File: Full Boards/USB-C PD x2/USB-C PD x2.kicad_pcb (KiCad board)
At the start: 4 copper layers, 96 x 136 mm, 161 parts, among them J1 Conn_02x05_Odd_Even, J2 Conn_01x05_Pin

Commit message: Changed the over voltage on the PMIC to under-voltage below 8.15V and over-voltage at 17.0V via a new voltage divider. This should save the TVS if the board is connected to a 24v supply.
Signed-off-by: digimer <digital.mermaid@gmail.com>
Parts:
- added R26: 47KR, Resistor_SMD:R_1206_3216Metric, F.Cu at (108.1, 153.2)
- R2: value 100KR -> 51.1KR
- TR1, TR10, TR11, TR12, TR2, TR3, TR4, TR5, TR6, TR7, TR8, TR9: value SOIC8_DMTH45M5LPSWQ-13_DIO -> Diodes Inc DMTH45M5LPSWQ-13
- moved R1 0.70 mm to (108.1, 148.6)
- moved R2 0.70 mm to (108.1, 150.9)
- moved C1 0.20 mm to (105.2, 155.5)
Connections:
- PMIC1 pad 3: -BATT -> Net-(PMIC1-OV)
- R2 pad 1: -BATT -> Net-(PMIC1-OV)
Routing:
- net Net-(PMIC1-OV): track 0.00 -> 16.2 mm
- net -BATT: track 100.8 -> 99.3 mm, vias 202 -> 200
- net Net-(HS1-D): track 46.8 -> 47.8 mm

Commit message: Updated PCB to apply the resistor KR -> kR corrections
Signed-off-by: digimer <digital.mermaid@gmail.com>
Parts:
- PR1, PR2, Rc2: value 2.2KR -> 2.2kR
- R17, R18, R19, R24: value 10KR -> 10kR
- R2: value 51.1KR -> 51.1kR
- R25: value xKR -> xkR
- R26: value 47KR -> 47kR
- R3: value 22.1KR -> 22.1kR
- Rc1: value 20KR -> 20kR
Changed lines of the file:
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@@
 			)
 		)
-		(property "Value" "22.1KR"
+		(property "Value" "22.1kR"
 			(at 0 1.83 0)
 			(layer "F.Fab")
@@
 			)
 		)
-		(property "Datasheet" ""
+		(property "Datasheet" "https://www.seielect.com/catalog/SEI-RNCP.pdf"
 			(at 0 0 0)
 			(layer "F.Fab")
@@
 			)
 		)
-		(property "Description" "RNCP1206FTD100K 100KR 0.5W"
+		(property "Description" "22.1 kOhms ±1% 0.5W, 1/2W Chip Resistor 1206 (3216 Metric) Anti-Sulfur Thin Film"
 			(at 0 0 0)
 			(layer "F.Fab")
@@
 			)
 		)
+		(property "Part" "Stackpole RNCP1206FTD22K1"
+			(at 0 0 180)
+			(unlocked yes)
+			(layer "F.Fab")
+			(hide yes)
+			(effects
+				(font
+					(size 1 1)
+					(thickness 0.15)
+				)
+			)
+		)
 		(property ki_fp_filters "R_*")
 		(sheetname "/")
@@
 			)
 		)
-		(property "Value" "10KR"
+		(property "Value" "10kR"
 			(at 0 1.83 90)
 			(layer "F.Fab")
@@
 			)
 		)
-		(property "Value" "2.2KR"
+		(property "Value" "2.2kR"
 			(at 0 1.83 0)
 			(layer "F.Fab")
@@
 			)
 		)
-		(property "Value" "xKR"
+		(property "Value" "xkR"
 			(at 0 4.1 0)
 			(unlocked yes)
@@
 			)
 		)
-		(property "Value" "2.2KR"
+		(property "Value" "2.2kR"
 			(at 0 1.83 90)
 			(layer "F.Fab")
@@
 			)
 		)
-		(property "Value" "20KR"
+		(property "Value" "20kR"
 			(at 0 1.83 90)
 			(layer "F.Fab")
@@
 			)
 		)
-		(property "Value" "2.2KR"
+		(property "Value" "2.2kR"
 			(at 0 1.83 0)
 			(layer "F.Fab")
@@
 			)
 		)
-		(property "Value" "10KR"
+		(property "Value" "10kR"
 			(at 0 4.1 0)
 			(unlocked yes)
@@
 			)
 		)
-		(property "Value" "47KR"
+		(property "Value" "47kR"
 			(at 0 1.83 0)
 			(layer "F.Fab")
@@
 			)
 		)
-		(property "Value" "51.1KR"
+		(property "Value" "51.1kR"
 			(at 0 1.83 0)
 			(layer "F.Fab")
@@
 			)
 		)
-		(property "Value" "10KR"
+		(property "Value" "10kR"
 			(at 0 1.83 90)
 			(layer "F.Fab")
@@
 			)
 		)
-		(property "Value" "10KR"
+		(property "Value" "10kR"
 			(at 0 1.83 90)
 			(layer "F.Fab")
@@
 	)
 	(segment
+		(start 104 151.79)
+		(end 104 152.8395)
+		(width 0.2)
+		(layer "F.Cu")
+		(net "Net-(PMIC1-OV)")
+	)
+	(segment
+		(start 109.5625 155.2375)
+		(end 109.5625 153.2)
+		(width 0.2)
+		(layer "F.Cu")
+		(net "Net-(PMIC1-OV)")
+	)
+	(segment
+		(start 103.5 156.6)
+		(end 108.2 156.6)
+		(width 0.2)
+		(layer "F.Cu")
+		(net "Net-(PMIC1-OV)")
+	)
+	(segment
+		(start 103.2 156.3)
+		(end 103.5 156.6)
+		(width 0.2)
+		(layer "F.Cu")
+		(net "Net-(PMIC1-OV)")
+	)
+	(segment
+		(start 104 152.8395)
+		(end 103.2 153.6395)
+		(width 0.2)
+		(layer "F.Cu")
+		(net "Net-(PMIC1-OV)")
+	)
+	(segment
+		(start 103.2 153.6395)
+		(end 103.2 156.3)
+		(width 0.2)
+		(layer "F.Cu")
+		(net "Net-(PMIC1-OV)")
+	)
+	(segment
+		(start 109.5625 153.2)
+		(end 109.5625 150.9)
+		(width 0.2)
+		(layer "F.Cu")
+		(net "Net-(PMIC1-OV)")
+	)
+	(segment
+		(start 108.2 156.6)
+		(end 109.5625 155.2375)
+		(width 0.2)
+		(layer "F.Cu")
+		(net "Net-(PMIC1-OV)")
+	)
+	(segment
 		(start 103.5 151.79)
 		(end 103.5 150.85)
@@
 		(net "Net-(TR7-G)")
 	)
-	(segment
-		(start 104 151.79)
-		(end 104 152.8395)
-		(width 0.2)
-		(layer "F.Cu")
-		(net "Net-(PMIC1-OV)")
-	)
-	(segment
-		(start 109.5625 155.2375)
-		(end 109.5625 153.2)
-		(width 0.2)
-		(layer "F.Cu")
-		(net "Net-(PMIC1-OV)")
-	)
-	(segment
-		(start 103.5 156.6)
-		(end 108.2 156.6)
-		(width 0.2)
-		(layer "F.Cu")
-		(net "Net-(PMIC1-OV)")
-	)
-	(segment
-		(start 103.2 156.3)
-		(end 103.5 156.6)
-		(width 0.2)
-		(layer "F.Cu")
-		(net "Net-(PMIC1-OV)")
-	)
-	(segment
-		(start 104 152.8395)
-		(end 103.2 153.6395)
-		(width 0.2)
-		(layer "F.Cu")
-		(net "Net-(PMIC1-OV)")
-	)
-	(segment
-		(start 103.2 153.6395)
-		(end 103.2 156.3)
-		(width 0.2)
-		(layer "F.Cu")
-		(net "Net-(PMIC1-OV)")
-	)
-	(segment
-		(start 109.5625 153.2)
-		(end 109.5625 150.9)
-		(width 0.2)
-		(layer "F.Cu")
-		(net "Net-(PMIC1-OV)")
-	)
-	(segment
-		(start 108.2 156.6)
-		(end 109.5625 155.2375)
-		(width 0.2)
-		(layer "F.Cu")
-		(net "Net-(PMIC1-OV)")
-	)
 	(zone

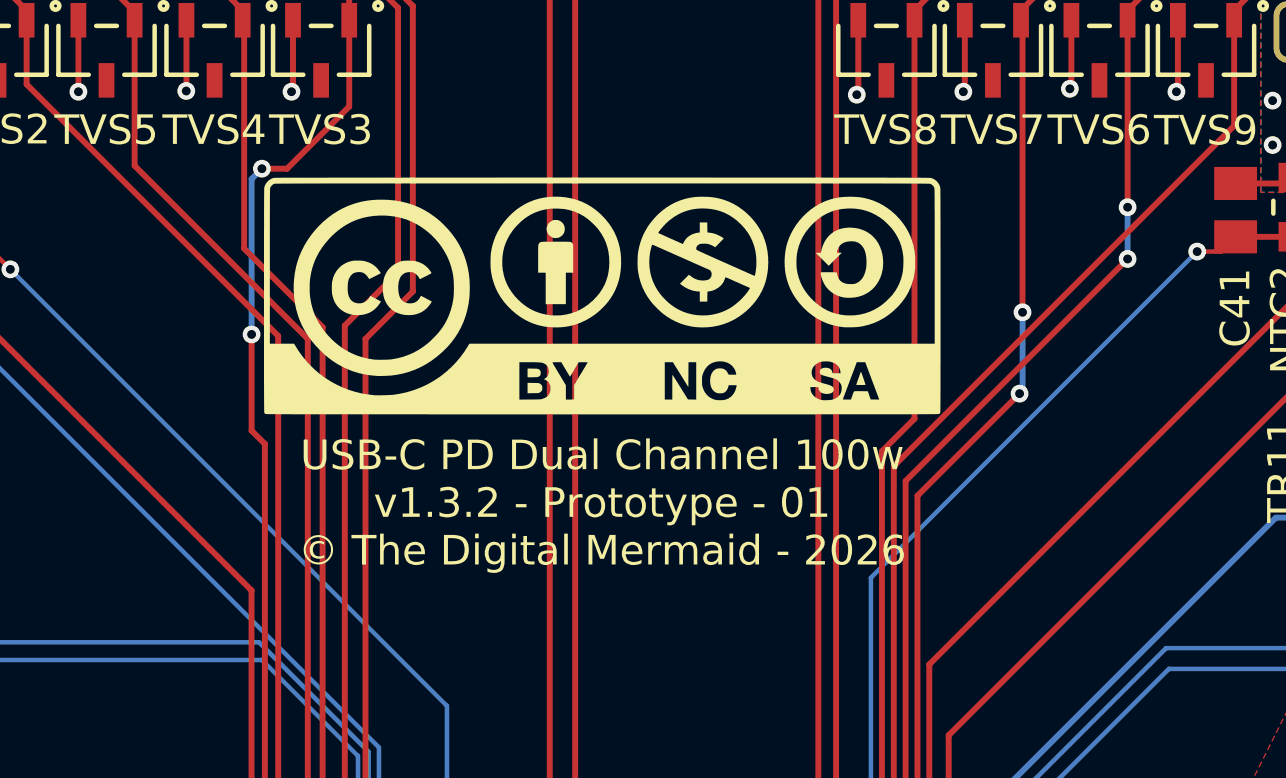
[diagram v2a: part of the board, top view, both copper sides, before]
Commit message: Changed the license to CERN-OHL-W v2.
Signed-off-by: digimer <digital.mermaid@gmail.com>
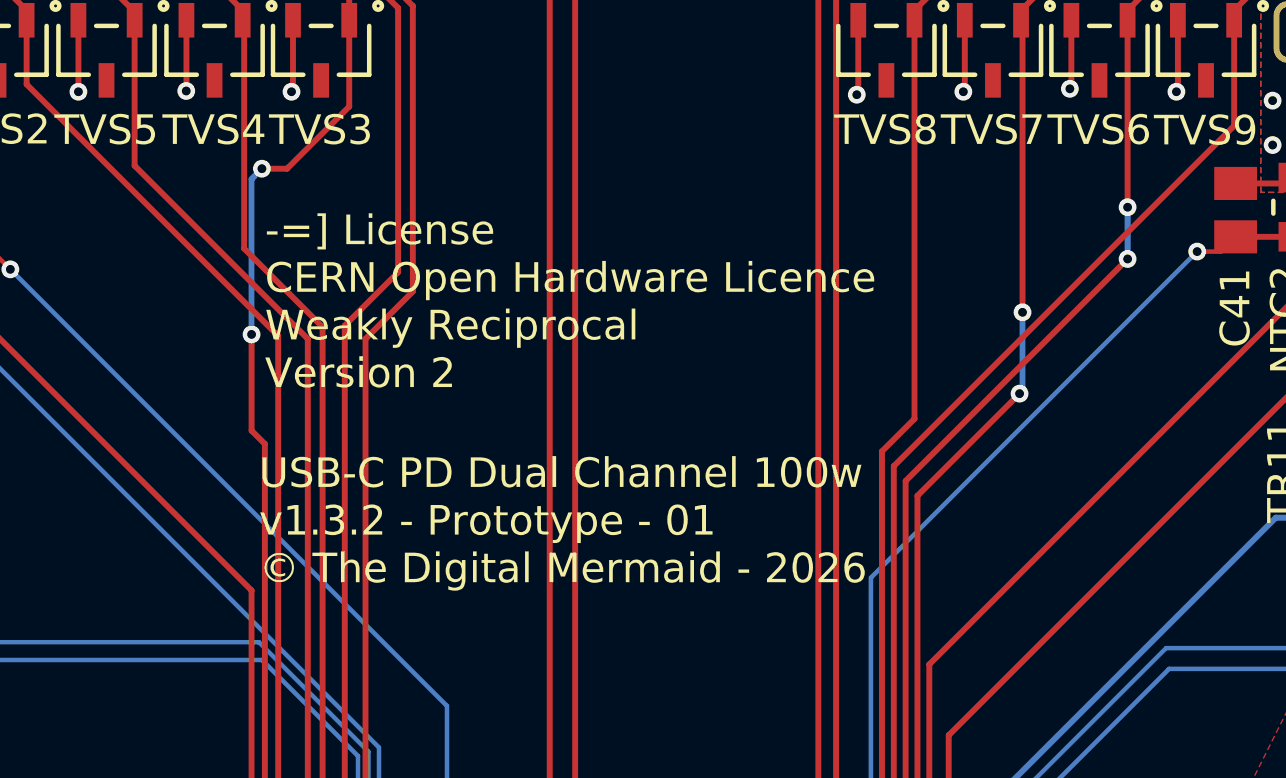
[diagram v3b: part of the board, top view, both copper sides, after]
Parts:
- removed the G*** at (100.0, 55.8)
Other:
- board text added: "-=] License CERN Open Hardware Licence Weakly Reciprocal Version 2"
